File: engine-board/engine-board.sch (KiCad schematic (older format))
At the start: 17 parts, among them J101 SD Card, U101 Teensy3.6_All_Pins, U102 FEATHER_M0_BASIC_PROTO

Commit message: Verions 1.0 done + ordered
added routes, submitted order
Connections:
- net labels added: gps_pss
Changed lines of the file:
@@
 Text Label 850  3050 2    50   ~ 0
 rs232_gnd
+Text Label 4600 900  2    50   ~ 0
+gps_pss
+Text Label 1600 6550 2    50   ~ 0
+gps_pss
 $EndSCHEMATC

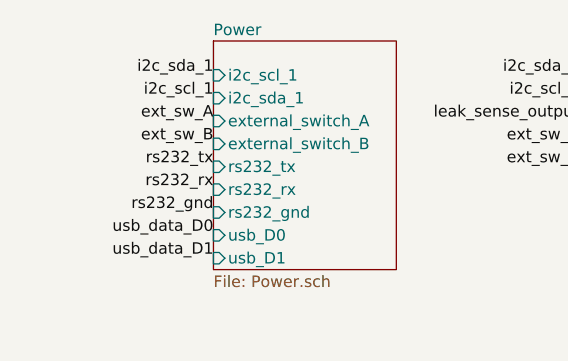
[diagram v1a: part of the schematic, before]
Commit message: board smaller
PCB V0.1 Errata:

- [QUESTION: - it looks like 12 on website] polulu 2814 has 16 pin footprint instead of 12...  AAACK!!!
- 5v and 3.3v traces could be wider
- [FIXED] fail: going into the power schematic scl + sda are swapped...
- [FIXED - moved to miniofit] pump controller silkscreen is wrong
- [FIXED] NOTE: just switch ALL to the minifit??
- [FIXED - will be on top, but not needed now] ADD: Ethernet connection from the teensy to the host computer board.
- [FIXED - going to use Qwiic) 9 Axis Mopak: wrong footprint - holes too small, spacing seems good, create outline as it bumps into feather header
- [FIXED] RV1805:  power + GND swapped... and I can’t seem to find them.
- [FIXED] 2 pressure sensors, the same i2c address... rerouted to 2nd i2c port on teensy
- [NOT NEEDED - adding display] Add RGB LED... it will be helpful for debugging.
- [FIXED - kindof - moved to micro-fit, might need to wire this directly to bulkhead] Turbine ferrules for power are 12 gauge - need bigger screw terminals if that is the connection method
- [FIXED] Feather footprint - lookup exactly what feather boards need for support..
- [FIXED] pump_motor_pwm is not connected to the TEENSY!!  blerg.  (jumper to pin 13 of feather for now)
- [FIXED - added FET] Maxon 70/30 POWER?  Think about power FET or ‘sleep’ to turn it off.
- [FIXED - added to bulkhead connector] Teensy 4.1 Program + ON/OFF pins - research how to extend these
- [TODO] remove VL6180 range sensor
- [LATER - will add to cost.. possibly remove?] put battery on back side
- add silkscreen for polulu
- [FIXED] Reorganize connectors:
    - Pump motor connectors go on end - attached in closing
    - bulkhead connectors go on side as they will always be attached
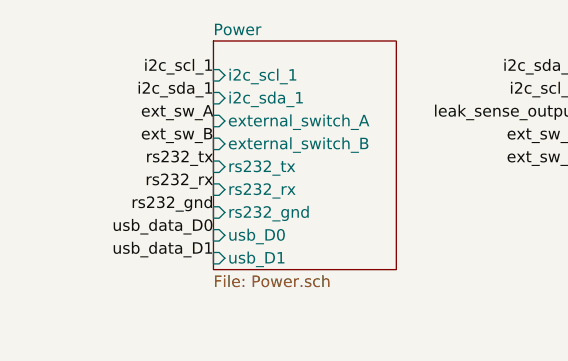
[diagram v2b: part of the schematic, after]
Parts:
- BT101: Link (none) -> https://www.digikey.com/en/products/detail/keystone-electro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; MANUFACTURER (none) -> Keystone; MPN (none) -> 1060; Price (none) -> 1.63
- J101: MATE_Link (none) -> https://www.digikey.com/en/products/detail/molex/0901210128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; MATE_MPN (none) -> 0901210128; MATE_Price (none) -> 1.16
- U101: Link https://www.digikey.com/en/products/detail/DEV-14058/1568-1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 -> https://www.digikey.com/en/products/detail/adafruit-industr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; Link2 (none) -> https://www.digikey.com/en/products/detail/DEV-14058/1568-1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; MPN DEV-14058 -> 3883; MPN2 (none) -> DEV-14058; Manufacturer (none) -> Adafruit; Price 36.88 -> 1.25; Price2 (none) -> 36.88
- U102: Link (none) -> https://www.digikey.com/en/products/detail/adafruit-industr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; Link2 (none) -> https://www.adafruit.com/product/4650; MANUFACTURER Adafruit -> (none); MPN (none) -> 2886; MPN2 (none) -> 4650; Manufacturer (none) -> Adafruit; Price (none) -> 0.95; Price2 (none) -> 14.95
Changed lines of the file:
@@
 F 2 "Module:ADAFRUIT_FEATHER" H 7700 5550 50  0001 L BNN
 F 3 "" H 7700 5550 50  0001 L BNN
-F 4 "Adafruit" H 7700 5550 50  0001 L BNN "MANUFACTURER"
+F 4 "" H 7700 5550 50  0001 L BNN "MANUFACTURER"
 F 5 "Manufacturer Recommendation" H 7700 5550 50  0001 L BNN "STANDARD"
+F 6 "https://www.digikey.com/en/products/detail/adafruit-industries-llc/2886/5823440" H 7700 5550 50  0001 C CNN "Link"
+F 7 "https://www.adafruit.com/product/4650" H 7700 5550 50  0001 C CNN "Link2"
+F 8 "14.95" H 7700 5550 50  0001 C CNN "Price2"
+F 9 "2886" H 7700 5550 50  0001 C CNN "MPN"
+F 10 "4650" H 7700 5550 50  0001 C CNN "MPN2"
+F 11 "Adafruit" H 7700 5550 50  0001 C CNN "Manufacturer"
+F 12 "0.95" H 7700 5550 50  0001 C CNN "Price"
 	1    7700 5550
 	1    0    0    -1
@@
 F 8 "https://www.adafruit.com/product/254" H 9450 1200 50  0001 C CNN "Link2"
 F 9 "7.50" H 9450 1200 50  0001 C CNN "Price2"
+F 10 "https://www.digikey.com/en/products/detail/molex/0901210128/760817?s=N4IgTCBcDaIJwAYCMYnLADhAXQL5A" H 9450 1200 50  0001 C CNN "MATE_Link"
+F 11 "0901210128" H 9450 1200 50  0001 C CNN "MATE_MPN"
+F 12 "1.16" H 9450 1200 50  0001 C CNN "MATE_Price"
 	1    9450 1200
 	1    0    0    -1
@@
 Text Label 2800 950  2    50   ~ 0
 leak_sense_output
+Text Label 1200 750  2    50   ~ 0
+i2c_scl_1
 Text Label 1200 850  2    50   ~ 0
-i2c_scl_1
-Text Label 1200 750  2    50   ~ 0
 i2c_sda_1
 Text Label 4600 1100 2    50   ~ 0
@@
 F 2 "Symbol:Teensy35_36" H 2750 5250 60  0000 C CNN
 F 3 "" H 2750 5250 60  0000 C CNN
-F 4 "DEV-14058" H 2750 5200 50  0001 C CNN "MPN"
-F 5 "36.88" H 2750 5200 50  0001 C CNN "Price"
-F 6 "https://www.digikey.com/en/products/detail/DEV-14058/1568-1465-ND/6569369?itemSeq=383715082" H 2750 5200 50  0001 C CNN "Link"
+F 4 "3883" H 2750 5200 50  0001 C CNN "MPN"
+F 5 "1.25" H 2750 5200 50  0001 C CNN "Price"
+F 6 "https://www.digikey.com/en/products/detail/adafruit-industries-llc/3883/11201426?s=N4IgTCBcDaIC4FMEDsDOBPEBdAvkA" H 2750 5200 50  0001 C CNN "Link"
+F 7 "https://www.digikey.com/en/products/detail/DEV-14058/1568-1465-ND/6569369?itemSeq=383715082" H 2750 5200 50  0001 C CNN "Link2"
+F 8 "36.88" H 2750 5200 50  0001 C CNN "Price2"
+F 9 "DEV-14058" H 2750 5200 50  0001 C CNN "MPN2"
+F 10 "Adafruit" H 2750 5200 50  0001 C CNN "Manufacturer"
 	1    2750 5200
 	1    0    0    -1
@@
 F 2 "Battery:BatteryHolder_Keystone_1060_1x2032" V 750 5610 50  0001 C CNN
 F 3 "~" V 750 5610 50  0001 C CNN
+F 4 "https://www.digikey.com/en/products/detail/keystone-electronics/1060/303556" H 750 5550 50  0001 C CNN "Link"
+F 5 "1060" H 750 5550 50  0001 C CNN "MPN"
+F 6 "" H 750 5550 50  0001 C CNN "Manufacturer"
+F 7 "1.63" H 750 5550 50  0001 C CNN "Price"
+F 8 "Keystone" H 750 5550 50  0001 C CNN "MANUFACTURER"
 	1    750  5550
 	1    0    0    -1
